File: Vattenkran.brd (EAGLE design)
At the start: 100 x 80 mm, 28 parts, among them J1 Battery, J2 Solar, J3 Valve, J4 Wakeup Button, Q2 32KHz

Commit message: Layout
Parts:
- removed D1, D2, D3: BAT19, diode:DO35-10
- removed J1: Battery, SparkFun-Connectors:1X02_LONGPADS
- removed J2: Solar, SparkFun-Connectors:1X02_LONGPADS
- removed J3: Valve, SparkFun-Connectors:1X02_LONGPADS
- removed J4: Wakeup Button, SparkFun-Connectors:1X02_LONGPADS
- removed LED1: GREEN, led:LED3MM
- removed R1: 1M, resistor:R0805
- removed R3: 3K3, resistor:R0805
- removed U$10: 500mA, fuse:MF-SMDF050
- removed U$11, U$3: MF-SMDF150, fuse:MF-SMDF050
- removed U$2: BATTERY_CHARGER, breakout-modules:BATTERY_CHARGER
- removed U$5: QSKJ_BOOST_MODULE, breakout-modules:QSKJ_BOOST_MODULE
- removed U$6: XL6009_BOOST_MODULE, breakout-modules:XL6009_BOOST_MODULE
- removed U$8: LM2576HVS_BUCK_MODULE, breakout-modules:LM2576HVS_BUCK_MODULE
- removed U$9: FDS6675, Semiconductors:SO08
- added TP1, TP2, TP3: TPB1,27, testpad:B1,27
- moved LED2 79.3 mm to (15.6, 16.7), turned to 90 degrees
- moved R2 75.4 mm to (15.6, 21.7), turned to 90 degrees
- moved U$4 68.4 mm to (21.0, 16.0), turned to 270 degrees
- moved C2 61.6 mm to (22.1, 27.6), turned to 90 degrees
- moved C3 53.4 mm to (16.5, 57.5), turned to 90 degrees
- moved U$7 49.8 mm to (23.0, 42.0), turned to 90 degrees
- moved C1 45.9 mm to (32.0, 71.0), turned to 90 degrees
- moved Q2 41.0 mm to (39.2, 72.4), turned to 180 degrees
- moved SUPERCAP 40.3 mm to (31.8, 64.0), turned to 180 degrees
- moved U$1 32.2 mm to (39.5, 64.0), turned to 180 degrees
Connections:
- removed net BT_POWER_ENABLE: R1.2, U$9.4
- removed net N$1: D2.C, U$10.2, U$8.IN
- removed net N$2: U$2.V_IN, U$8.OUT
- removed net N$36: D3.C, U$11.2, U$2.V_BATT+
- removed net N$6: D1.C, U$3.1, U$6.V_OUT
- removed net N$9: LED1.K, R3.1
- removed net SOLAR: J2.2, U$10.1
- removed net VALVE: J3.2, U$3.2
- removed net V_BATT+: J1.2, U$11.1
- removed net V_UNREG: R1.1, U$2.V_OUT, U$5.V_IN, U$9.1, U$9.2, U$9.3
- removed net V_VALVE_UNREG: LED1.A, U$6.V_IN, U$9.5, U$9.6, U$9.7, U$9.8
- new net VALVE_ENABLE: TP2.TP, U$7.A0
- net BUTTON_WAKEUP_INT: now also TP3.TP; no longer J4.2
- net GND: no longer D1.A, D2.A, D3.A, J1.1, J2.1, J3.1, J4.1, R3.2, U$2.GND@1, U$2.GND@2, U$2.V_BATT-, U$5.GND@1, U$5.GND@2, U$6.V_IN_GND, U$6.V_OUT_GND, U$8.GND@1, U$8.GND@2
- net VCC33: no longer C3.1
- net VCC5: now also C3.1, TP1.TP; no longer U$5.V_OUT
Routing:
- net V_UNREG: track 103.4 -> 0.00 mm
- net N$2: track 68.6 -> 0.00 mm
- net BUTTON_WAKEUP_INT: track 50.7 -> 113.3 mm
- net VALVE_ENABLE: track 0.00 -> 52.3 mm, vias 0 -> 2
- net V_VALVE_UNREG: track 30.7 -> 0.00 mm
- net VCC5: track 61.8 -> 32.5 mm
- net N$36: track 26.7 -> 0.00 mm
- net BT_GND: track 0.00 -> 25.1 mm
- net N$1: track 24.4 -> 0.00 mm
- net N$6: track 14.3 -> 0.00 mm
- net VALVE: track 13.5 -> 0.00 mm
- net V_BATT+: track 7.27 -> 0.00 mm
- net BT_POWER_ENABLE: track 7.10 -> 0.00 mm
- net SOLAR: track 5.61 -> 0.00 mm
- net BT_STATE: track 43.3 -> 48.6 mm
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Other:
- board size 100 x 80 mm -> 65 x 80 mm

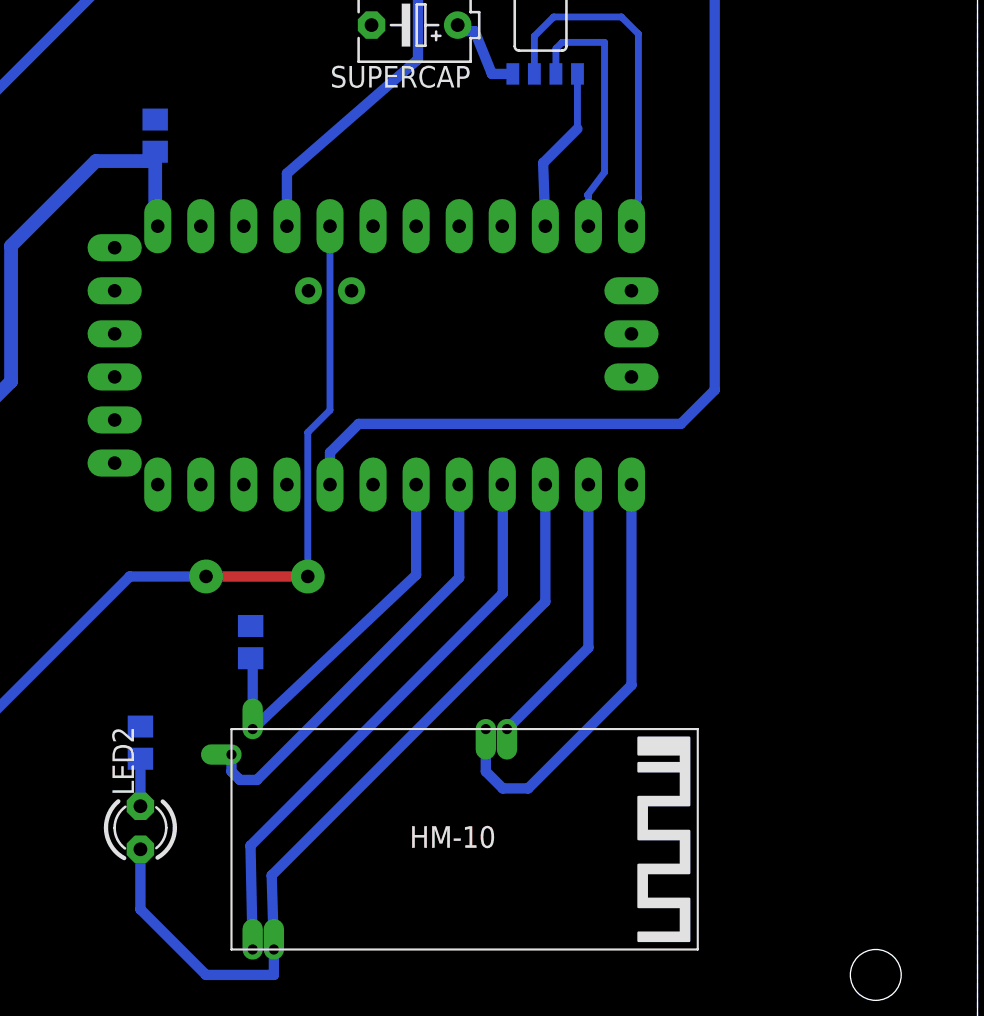
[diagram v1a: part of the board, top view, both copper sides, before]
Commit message: Fill to edge
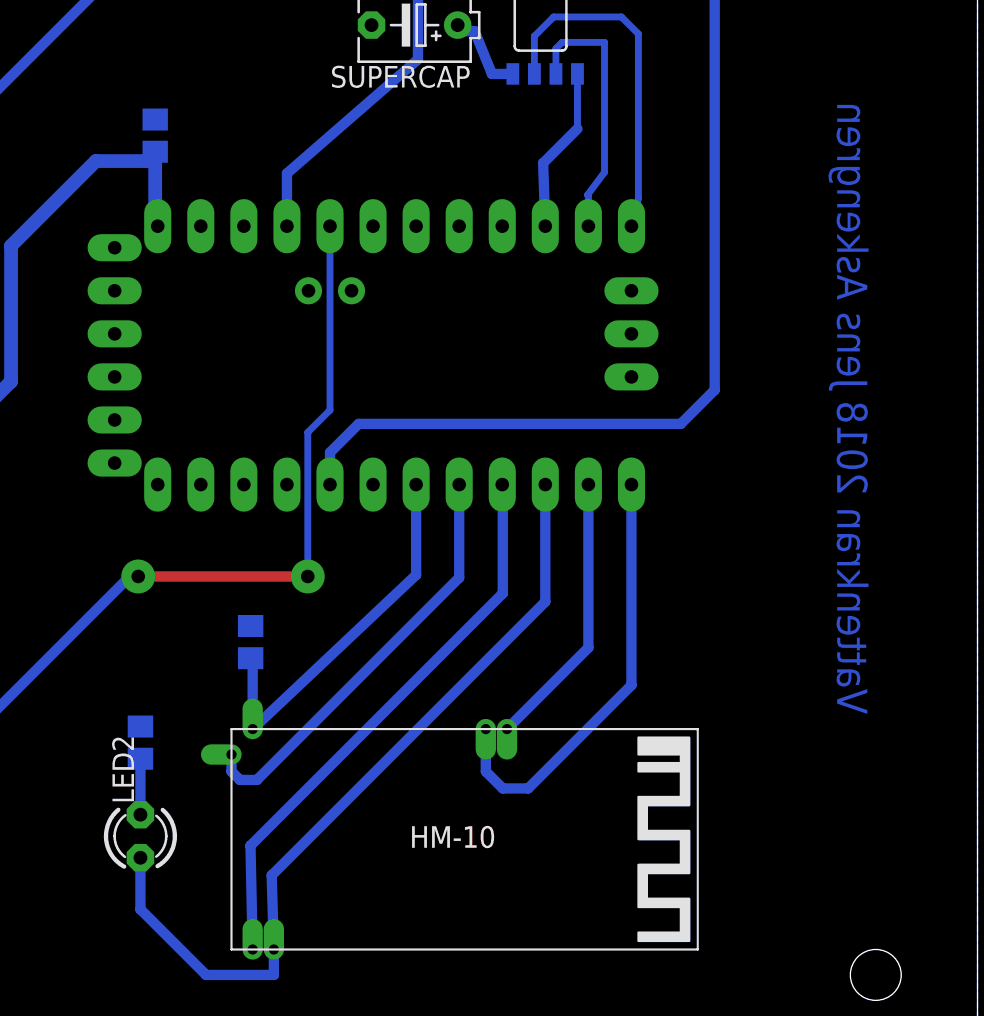
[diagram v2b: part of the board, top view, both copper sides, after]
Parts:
- moved LED2 0.50 mm to (15.6, 16.2)
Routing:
- net N$3: track 2.80 -> 3.30 mm
- net BT_STATE: track 48.6 -> 48.1 mm
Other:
- board text added: "Vattenkran 2018 Jens Askengren"
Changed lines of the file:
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@@
 <hole x="58" y="72" drill="3"/>
 <hole x="59" y="8" drill="3"/>
+<text x="58.5" y="59.5" size="1.778" layer="16" rot="MR270">Vattenkran 2018 Jens Askengren</text>
 </plain>
 <attributes>
@@
 <param name="mdViaViaSameLayer" value="6mil"/>
 <param name="mnLayersViaInSmd" value="2"/>
-<param name="mdCopperDimension" value="40mil"/>
+<param name="mdCopperDimension" value="0mil"/>
 <param name="mdDrill" value="6mil"/>
 <param name="mdSmdStop" value="0mil"/>
@@
 <element name="C2" library="resistor" library_urn="urn:adsk.eagle:library:348" package="C0805" package3d_urn="urn:adsk.eagle:package:26137/1" value="100nF" x="22.13" y="27.63" rot="MR90"/>
 <element name="C3" library="resistor" library_urn="urn:adsk.eagle:library:348" package="C0805" package3d_urn="urn:adsk.eagle:package:26137/1" value="100nF" x="16.5" y="57.5" rot="MR90"/>
-<element name="LED2" library="led" library_urn="urn:adsk.eagle:library:259" package="LED3MM" package3d_urn="urn:adsk.eagle:package:15797/1" value="GREEN" x="15.63" y="16.68" rot="R90"/>
+<element name="LED2" library="led" library_urn="urn:adsk.eagle:library:259" package="LED3MM" package3d_urn="urn:adsk.eagle:package:15797/1" value="GREEN" x="15.63" y="16.18" rot="R90"/>
 <element name="Q2" library="adafruit" package="TC38H" value="32KHz" x="39.23" y="72.42" rot="R180">
 <attribute name="MF" value="" x="39.23" y="72.42" size="1.778" layer="27" rot="R180" display="off"/>
@@
 <contactref element="C3" pad="2"/>
 <contactref element="C2" pad="2"/>
-<polygon width="0.508" layer="16" isolate="1.016">
+<polygon width="0" layer="16" isolate="1.016">
 <vertex x="0" y="80"/>
 <vertex x="65" y="80"/>
@@
 <vertex x="0" y="0"/>
 </polygon>
-<wire x1="22.13" y1="28.58" x2="24.27" y2="36.92" width="0" layer="19" extent="16-16"/>
-<wire x1="19.19" y1="52.16" x2="24.27" y2="36.92" width="0" layer="19" extent="1-1"/>
 </signal>
 <signal name="BT_RX">
@@
 <wire x1="23.5" y1="8" x2="19.5" y2="8" width="0.6096" layer="16"/>
 <wire x1="19.5" y1="8" x2="15.63" y2="11.87" width="0.6096" layer="16"/>
-<wire x1="15.63" y1="11.87" x2="15.63" y2="15.41" width="0.6096" layer="16"/>
+<wire x1="15.63" y1="11.87" x2="15.63" y2="14.91" width="0.6096" layer="16"/>
 </signal>
 <signal name="VCC5">
@@
 <contactref element="R2" pad="1"/>
 <contactref element="LED2" pad="K"/>
-<wire x1="15.63" y1="17.95" x2="15.63" y2="20.75" width="0.6096" layer="16"/>
+<wire x1="15.63" y1="17.45" x2="15.63" y2="20.75" width="0.6096" layer="16"/>
 </signal>
 <signal name="N$4">
@@
 <wire x1="25.5" y1="40" x2="25.5" y2="31.5" width="0.4064" layer="16"/>
 <via x="25.5" y="31.5" extent="1-16" drill="0.8" diameter="2"/>
-<wire x1="25.5" y1="31.5" x2="19.5" y2="31.5" width="0.6096" layer="1"/>
-<via x="19.5" y="31.5" extent="1-16" drill="0.8" diameter="2"/>
-<wire x1="19.5" y1="31.5" x2="15" y2="31.5" width="0.6096" layer="16"/>
+<wire x1="25.5" y1="31.5" x2="15.5" y2="31.5" width="0.6096" layer="1"/>
+<via x="15.5" y="31.5" extent="1-16" drill="0.8" diameter="2"/>
+<wire x1="15.5" y1="31.5" x2="15" y2="31.5" width="0.6096" layer="16"/>
 <wire x1="15" y1="31.5" x2="3.5" y2="20" width="0.6096" layer="16"/>
 <wire x1="3.5" y1="20" x2="-0.1792" y2="20" width="0.6096" layer="16"/>

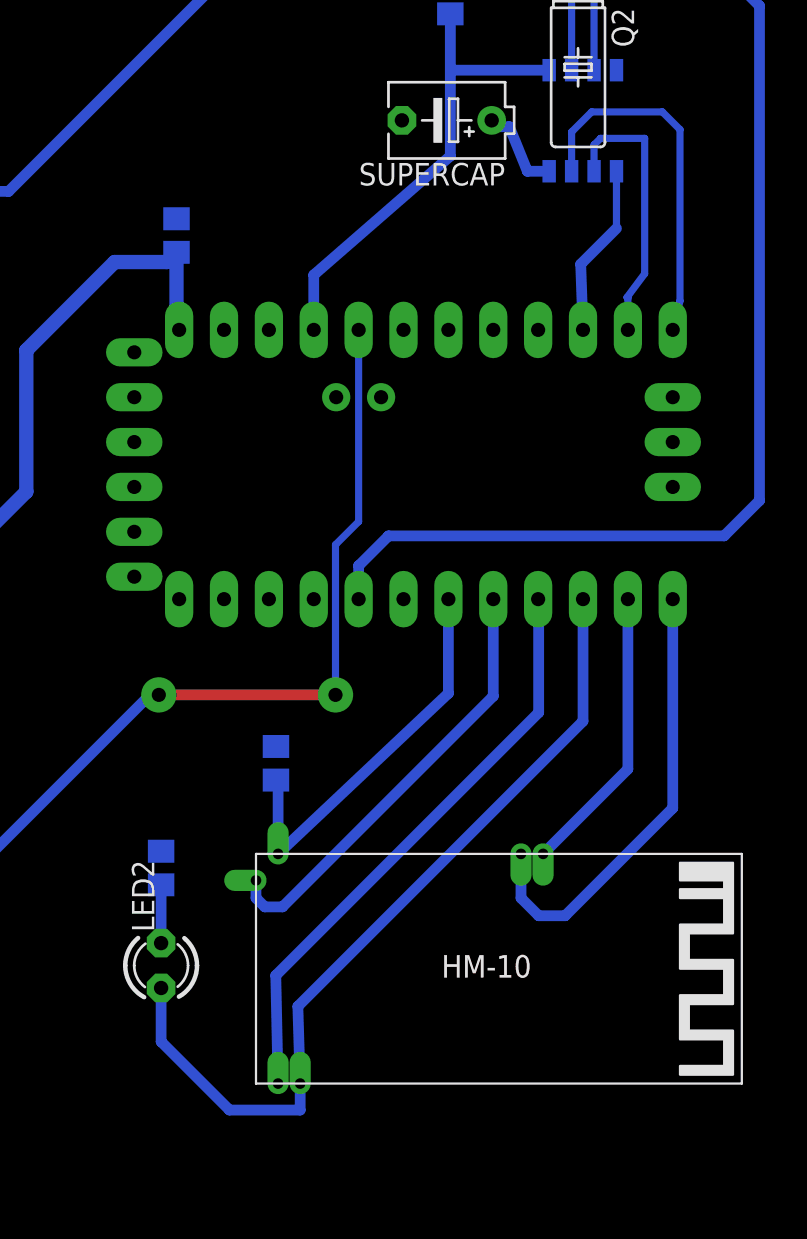
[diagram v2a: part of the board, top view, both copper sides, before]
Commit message: Replaced PTC
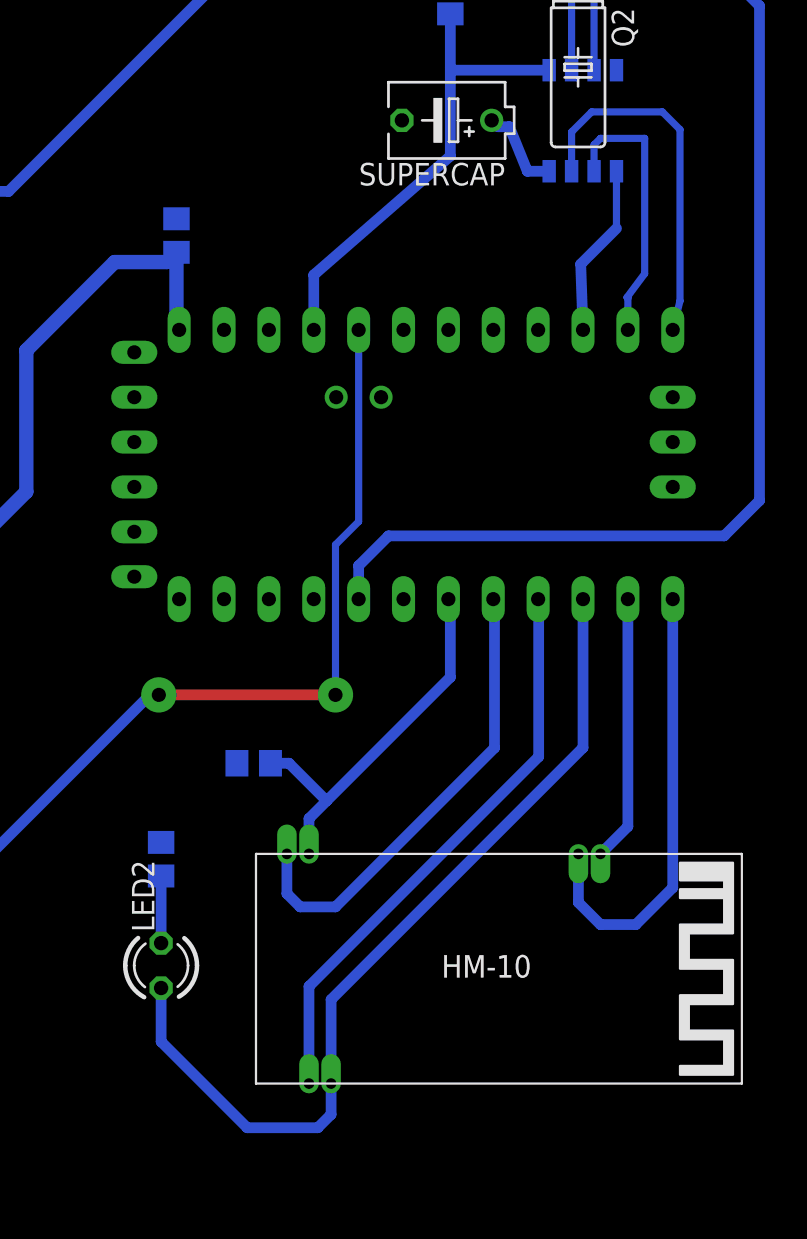
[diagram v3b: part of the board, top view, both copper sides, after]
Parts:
- moved C2 1.26 mm to (20.9, 27.6), turned to 0 degrees
- moved R2 0.50 mm to (15.6, 22.2)
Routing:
- net BT_STATE: track 48.1 -> 50.1 mm
- net BT_GND: track 25.1 -> 26.5 mm
- net BT_TX: track 16.4 -> 15.1 mm
- net BT_VCC33: track 22.8 -> 21.8 mm
- net BT_BRK: track 33.6 -> 32.8 mm
- net N$3: track 3.30 -> 3.80 mm
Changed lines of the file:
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@@
 <param name="msMicroVia" value="9.99mm"/>
 <param name="msBlindViaRatio" value="0.5"/>
-<param name="rvPadTop" value="0.5"/>
+<param name="rvPadTop" value="0.25"/>
 <param name="rvPadInner" value="0.25"/>
 <param name="rvPadBottom" value="0.25"/>
@@
 <param name="dpGapFactor" value="2.5"/>
 <param name="checkAngle" value="0"/>
-<param name="checkFont" value="1"/>
+<param name="checkFont" value="0"/>
 <param name="checkRestrict" value="1"/>
 <param name="checkStop" value="0"/>
@@
 <elements>
 <element name="C1" library="resistor" library_urn="urn:adsk.eagle:library:348" package="C0805" package3d_urn="urn:adsk.eagle:package:26137/1" value="100nF" x="32" y="71" rot="MR90"/>
-<element name="C2" library="resistor" library_urn="urn:adsk.eagle:library:348" package="C0805" package3d_urn="urn:adsk.eagle:package:26137/1" value="100nF" x="22.13" y="27.63" rot="MR90"/>
+<element name="C2" library="resistor" library_urn="urn:adsk.eagle:library:348" package="C0805" package3d_urn="urn:adsk.eagle:package:26137/1" value="100nF" x="20.87" y="27.63" rot="MR0"/>
 <element name="C3" library="resistor" library_urn="urn:adsk.eagle:library:348" package="C0805" package3d_urn="urn:adsk.eagle:package:26137/1" value="100nF" x="16.5" y="57.5" rot="MR90"/>
 <element name="LED2" library="led" library_urn="urn:adsk.eagle:library:259" package="LED3MM" package3d_urn="urn:adsk.eagle:package:15797/1" value="GREEN" x="15.63" y="16.18" rot="R90"/>
@@
 <attribute name="OC_NEWARK" value="unknown" x="39.23" y="72.42" size="1.778" layer="27" rot="R180" display="off"/>
 </element>
-<element name="R2" library="resistor" library_urn="urn:adsk.eagle:library:348" package="R0805" package3d_urn="urn:adsk.eagle:package:26059/1" value="3K3" x="15.63" y="21.7" rot="MR90"/>
+<element name="R2" library="resistor" library_urn="urn:adsk.eagle:library:348" package="R0805" package3d_urn="urn:adsk.eagle:package:26059/1" value="3K3" x="15.63" y="22.2" rot="MR90"/>
 <element name="SUPERCAP" library="rcl" library_urn="urn:adsk.eagle:library:334" package="ETR2" package3d_urn="urn:adsk.eagle:package:23315/1" value="1F" x="31.8" y="64.02" rot="R180">
 <attribute name="SPICEPREFIX" value="C" x="31.8" y="64.02" size="1.778" layer="27" rot="R180" display="off"/>
@@
 <contactref element="U$4" pad="RX"/>
 <contactref element="U$7" pad="D9"/>
-<wire x1="36" y1="20" x2="37" y2="19" width="0.6096" layer="16"/>
-<wire x1="37" y1="19" x2="38.5" y2="19" width="0.6096" layer="16"/>
-<wire x1="38.5" y1="19" x2="44.59" y2="25.09" width="0.6096" layer="16"/>
-<wire x1="44.59" y1="25.09" x2="44.59" y2="36.92" width="0.6096" layer="16"/>
-<wire x1="36" y1="22.5" x2="36" y2="20" width="0.6096" layer="16"/>
+<wire x1="39.25" y1="22.5" x2="39.25" y2="19.75" width="0.6096" layer="16"/>
+<wire x1="39.25" y1="19.75" x2="40.5" y2="18.5" width="0.6096" layer="16"/>
+<wire x1="40.5" y1="18.5" x2="42.5" y2="18.5" width="0.6096" layer="16"/>
+<wire x1="42.5" y1="18.5" x2="44.59" y2="20.59" width="0.6096" layer="16"/>
+<wire x1="44.59" y1="20.59" x2="44.59" y2="36.92" width="0.6096" layer="16"/>
 </signal>
 <signal name="BT_TX">
 <contactref element="U$4" pad="TX"/>
 <contactref element="U$7" pad="D8"/>
-<wire x1="37.25" y1="22.5" x2="42.05" y2="27.3" width="0.6096" layer="16"/>
-<wire x1="42.05" y1="27.3" x2="42.05" y2="36.92" width="0.6096" layer="16"/>
+<wire x1="40.5" y1="22.5" x2="42.05" y2="24.05" width="0.6096" layer="16"/>
+<wire x1="42.05" y1="24.05" x2="42.05" y2="36.92" width="0.6096" layer="16"/>
 </signal>
 <signal name="BUTTON_WAKEUP_INT">
@@
 <contactref element="U$7" pad="D7"/>
 <contactref element="LED2" pad="A"/>
-<wire x1="23.5" y1="9.5" x2="23.37" y2="13.87" width="0.6096" layer="16"/>
-<wire x1="39.51" y1="30.01" x2="39.51" y2="36.92" width="0.6096" layer="16"/>
-<wire x1="23.37" y1="13.87" x2="39.51" y2="30.01" width="0.6096" layer="16"/>
-<wire x1="23.5" y1="9.5" x2="23.5" y2="8" width="0.6096" layer="16"/>
-<wire x1="23.5" y1="8" x2="19.5" y2="8" width="0.6096" layer="16"/>
-<wire x1="19.5" y1="8" x2="15.63" y2="11.87" width="0.6096" layer="16"/>
+<wire x1="25.25" y1="9.5" x2="25.25" y2="14.25" width="0.6096" layer="16"/>
+<wire x1="39.51" y1="28.51" x2="39.51" y2="36.92" width="0.6096" layer="16"/>
+<wire x1="25.25" y1="14.25" x2="39.51" y2="28.51" width="0.6096" layer="16"/>
+<wire x1="25.25" y1="9.5" x2="25.25" y2="7.75" width="0.6096" layer="16"/>
+<wire x1="25.25" y1="7.75" x2="24.5" y2="7" width="0.6096" layer="16"/>
+<wire x1="24.5" y1="7" x2="20.5" y2="7" width="0.6096" layer="16"/>
+<wire x1="20.5" y1="7" x2="15.63" y2="11.87" width="0.6096" layer="16"/>
 <wire x1="15.63" y1="11.87" x2="15.63" y2="14.91" width="0.6096" layer="16"/>
 </signal>
@@
 <contactref element="U$4" pad="BRK"/>
 <contactref element="U$7" pad="D6"/>
-<wire x1="22.25" y1="9.5" x2="22.12" y2="15.62" width="0.6096" layer="16"/>
-<wire x1="22.12" y1="15.62" x2="37" y2="30.5" width="0.6096" layer="16"/>
-<wire x1="37" y1="30.5" x2="37" y2="36.89" width="0.6096" layer="16"/>
+<wire x1="24" y1="9.5" x2="24" y2="15" width="0.6096" layer="16"/>
+<wire x1="24" y1="15" x2="37" y2="28" width="0.6096" layer="16"/>
+<wire x1="37" y1="28" x2="37" y2="36.89" width="0.6096" layer="16"/>
 <wire x1="37" y1="36.89" x2="36.97" y2="36.92" width="0.6096" layer="16"/>
 </signal>
@@
 <contactref element="U$4" pad="GND"/>
 <contactref element="U$7" pad="D5"/>
-<wire x1="21" y1="21" x2="21" y2="20" width="0.6096" layer="16"/>
-<wire x1="21" y1="20" x2="21.5" y2="19.5" width="0.6096" layer="16"/>
-<wire x1="21.5" y1="19.5" x2="22.5" y2="19.5" width="0.6096" layer="16"/>
-<wire x1="22.5" y1="19.5" x2="34.43" y2="31.43" width="0.6096" layer="16"/>
-<wire x1="34.43" y1="31.43" x2="34.43" y2="36.92" width="0.6096" layer="16"/>
+<wire x1="22.75" y1="22.5" x2="22.75" y2="20.25" width="0.6096" layer="16"/>
+<wire x1="22.75" y1="20.25" x2="23.5" y2="19.5" width="0.6096" layer="16"/>
+<wire x1="25.5" y1="19.5" x2="34.5" y2="28.5" width="0.6096" layer="16"/>
+<wire x1="34.5" y1="28.5" x2="34.5" y2="36.85" width="0.6096" layer="16"/>
+<wire x1="34.5" y1="36.85" x2="34.43" y2="36.92" width="0.6096" layer="16"/>
+<wire x1="23.5" y1="19.5" x2="25.5" y2="19.5" width="0.6096" layer="16"/>
 </signal>
 <signal name="BT_VCC33">
@@
 <contactref element="C2" pad="1"/>
 <contactref element="U$7" pad="D4"/>
-<wire x1="22.25" y1="22.5" x2="31.89" y2="31.59" width="0.6096" layer="16"/>
-<wire x1="31.89" y1="31.59" x2="31.89" y2="36.92" width="0.6096" layer="16"/>
-<wire x1="22.25" y1="22.5" x2="22.25" y2="26.56" width="0.6096" layer="16"/>
-<wire x1="22.25" y1="26.56" x2="22.13" y2="26.68" width="0.6096" layer="16"/>
+<wire x1="24" y1="22.5" x2="24" y2="24.5" width="0.6096" layer="16"/>
+<wire x1="24" y1="24.5" x2="25" y2="25.5" width="0.6096" layer="16"/>
+<wire x1="25" y1="25.5" x2="32" y2="32.5" width="0.6096" layer="16"/>
+<wire x1="32" y1="32.5" x2="32" y2="36.81" width="0.6096" layer="16"/>
+<wire x1="32" y1="36.81" x2="31.89" y2="36.92" width="0.6096" layer="16"/>
+<wire x1="21.82" y1="27.63" x2="22.87" y2="27.63" width="0.6096" layer="16"/>
+<wire x1="22.87" y1="27.63" x2="25" y2="25.5" width="0.6096" layer="16"/>
 </signal>
 <signal name="N$3">
 <contactref element="R2" pad="1"/>
 <contactref element="LED2" pad="K"/>
-<wire x1="15.63" y1="17.45" x2="15.63" y2="20.75" width="0.6096" layer="16"/>
+<wire x1="15.63" y1="17.45" x2="15.63" y2="21.25" width="0.6096" layer="16"/>
 </signal>
 <signal name="N$4">
